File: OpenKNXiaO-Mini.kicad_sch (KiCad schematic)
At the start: 10 parts, among them J1 Conn_KNX, J5 Conn_01x05, J6 Conn_01x05, J7 Conn_01x12, SW1 Prog BTN, U1 Seeeduino XIAO

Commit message: OpenKNXiaO - Final form and dimensions are now established.
Initial housing is startet. Dimensions could be changed later
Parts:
- GN1: footprint KNeoPix:NanoBCU_PinSocket_LowProfile -> KNeoPix:OpenKNX_BCU_V2.0
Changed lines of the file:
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@@
     (pin "2")
     (instances
-      (project "KNeoPiX_v1.3"
+      (project "OpenKNXiaO-Mini"
         (path "/e63e39d7-6ac0-4ffd-8aa3-1841a4541b55"
           (reference "JP4") (unit 1)
@@
     (pin "2")
     (instances
-      (project "KNeoPiX_v1.3"
+      (project "OpenKNXiaO-Mini"
         (path "/e63e39d7-6ac0-4ffd-8aa3-1841a4541b55"
           (reference "J1") (unit 1)
@@
     (pin "2")
     (instances
-      (project "KNeoPiX_v1.3"
+      (project "OpenKNXiaO-Mini"
         (path "/e63e39d7-6ac0-4ffd-8aa3-1841a4541b55"
           (reference "SW1") (unit 1)
@@
       (effects (font (size 1.27 1.27)) (justify left))
     )
-    (property "Footprint" "KNeoPix:NanoBCU_PinSocket_LowProfile" (at 23.368 56.896 0)
+    (property "Footprint" "KNeoPix:OpenKNX_BCU_V2.0" (at 23.368 56.896 0)
       (effects (font (size 1.27 1.27)) hide)
     )
@@
     (pin "7")
     (instances
-      (project "KNeoPiX_v1.3"
+      (project "OpenKNXiaO-Mini"
         (path "/e63e39d7-6ac0-4ffd-8aa3-1841a4541b55"
           (reference "GN1") (unit 1)
@@
     (pin "9")
     (instances
-      (project "KNeoPiX_v1.3"
+      (project "OpenKNXiaO-Mini"
         (path "/e63e39d7-6ac0-4ffd-8aa3-1841a4541b55"
           (reference "U1") (unit 1)
@@
     (pin "9")
     (instances
-      (project "KNeoPiX_v1.3"
+      (project "OpenKNXiaO-Mini"
         (path "/e63e39d7-6ac0-4ffd-8aa3-1841a4541b55"
           (reference "J7") (unit 1)
@@
     (pin "C")
     (instances
-      (project "KNeoPiX_v1.3"
+      (project "OpenKNXiaO-Mini"
         (path "/e63e39d7-6ac0-4ffd-8aa3-1841a4541b55"
           (reference "D3") (unit 1)
@@
     (pin "5")
     (instances
-      (project "KNeoPiX_v1.3"
+      (project "OpenKNXiaO-Mini"
         (path "/e63e39d7-6ac0-4ffd-8aa3-1841a4541b55"
           (reference "J5") (unit 1)
@@
     (pin "5")
     (instances
-      (project "KNeoPiX_v1.3"
+      (project "OpenKNXiaO-Mini"
         (path "/e63e39d7-6ac0-4ffd-8aa3-1841a4541b55"
           (reference "J6") (unit 1)
@@
     (pin "2")
     (instances
-      (project "KNeoPiX_v1.3"
+      (project "OpenKNXiaO-Mini"
         (path "/e63e39d7-6ac0-4ffd-8aa3-1841a4541b55"
           (reference "C7") (unit 1)

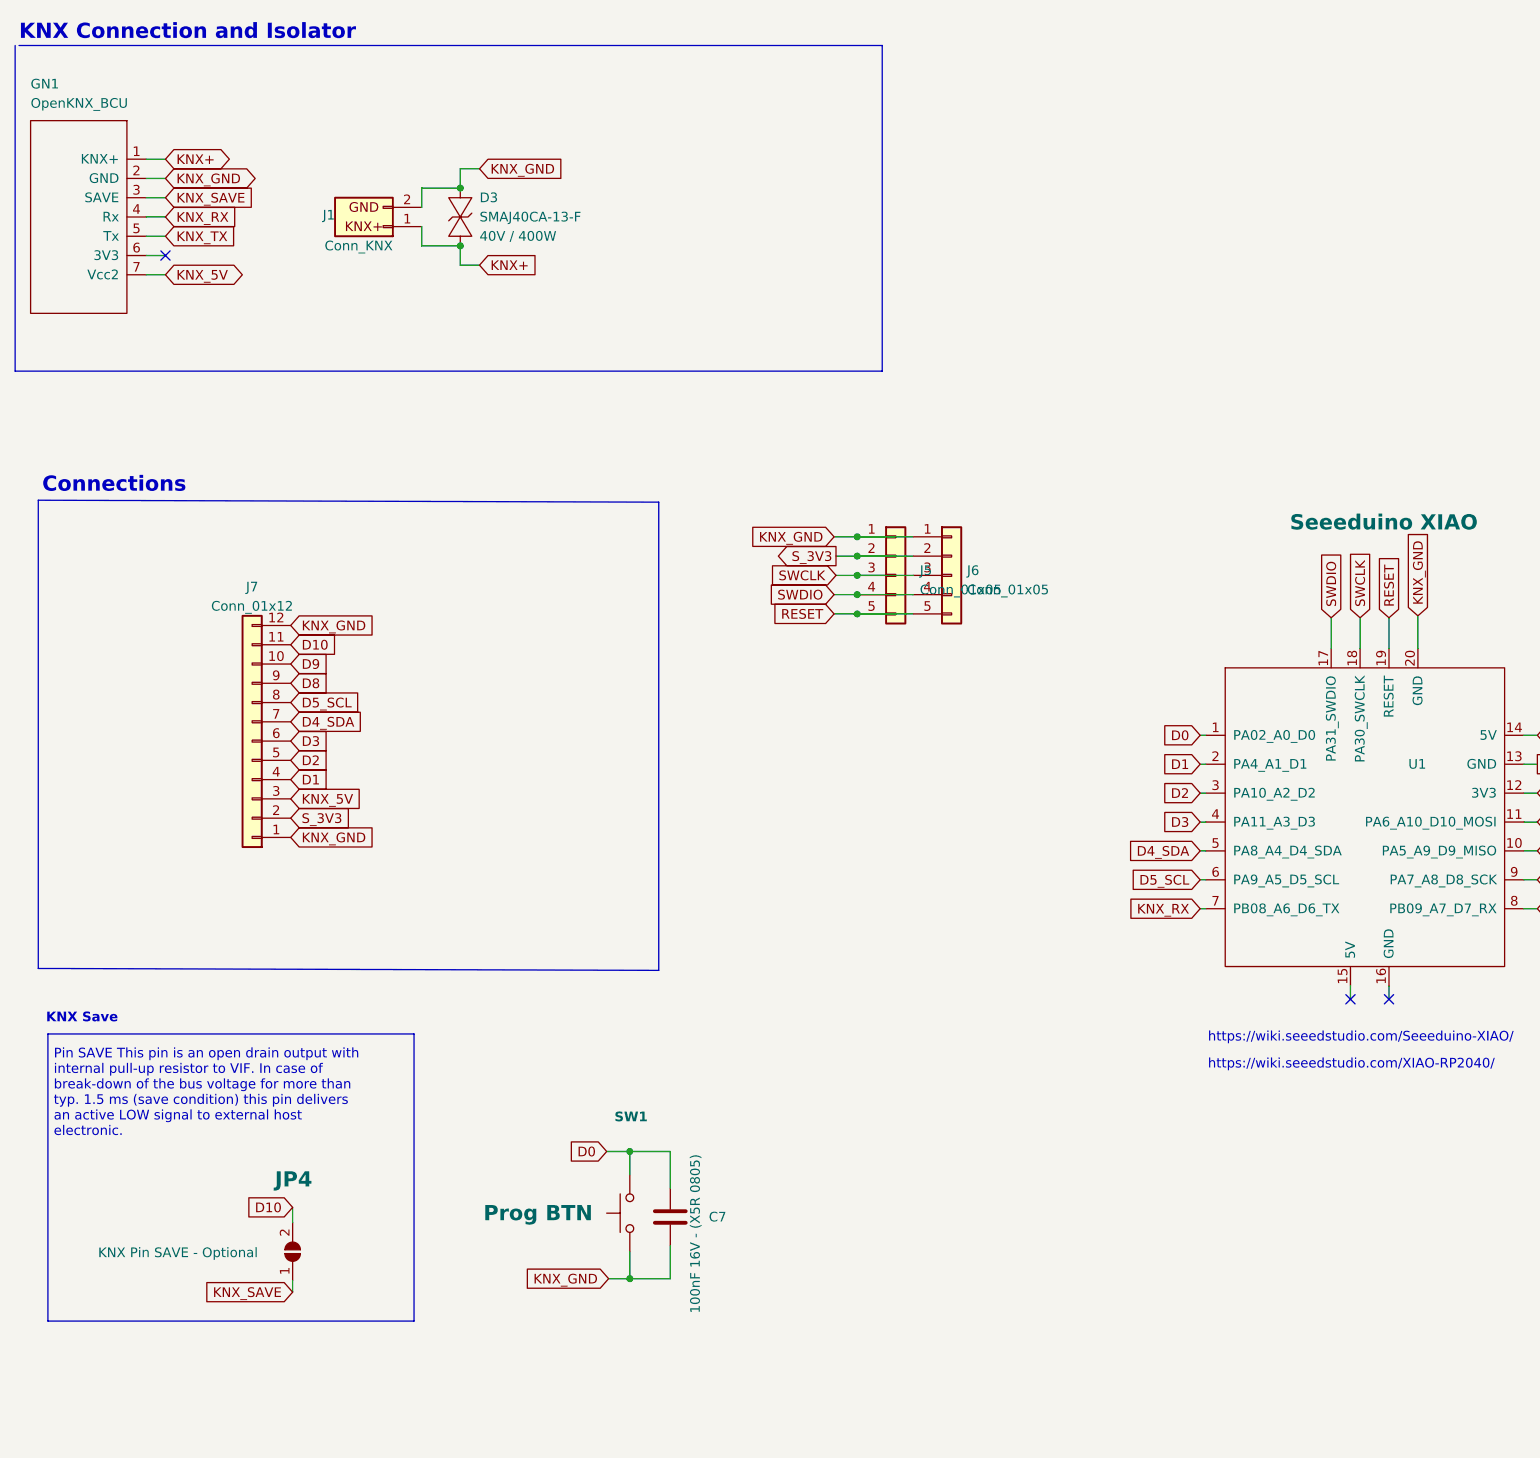
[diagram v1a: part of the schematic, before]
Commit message: Centered KNX connection and first routing
Updated low high profile (Pin-Header / Low BCU)
Removed SMA Diode. BCU has allready its own.
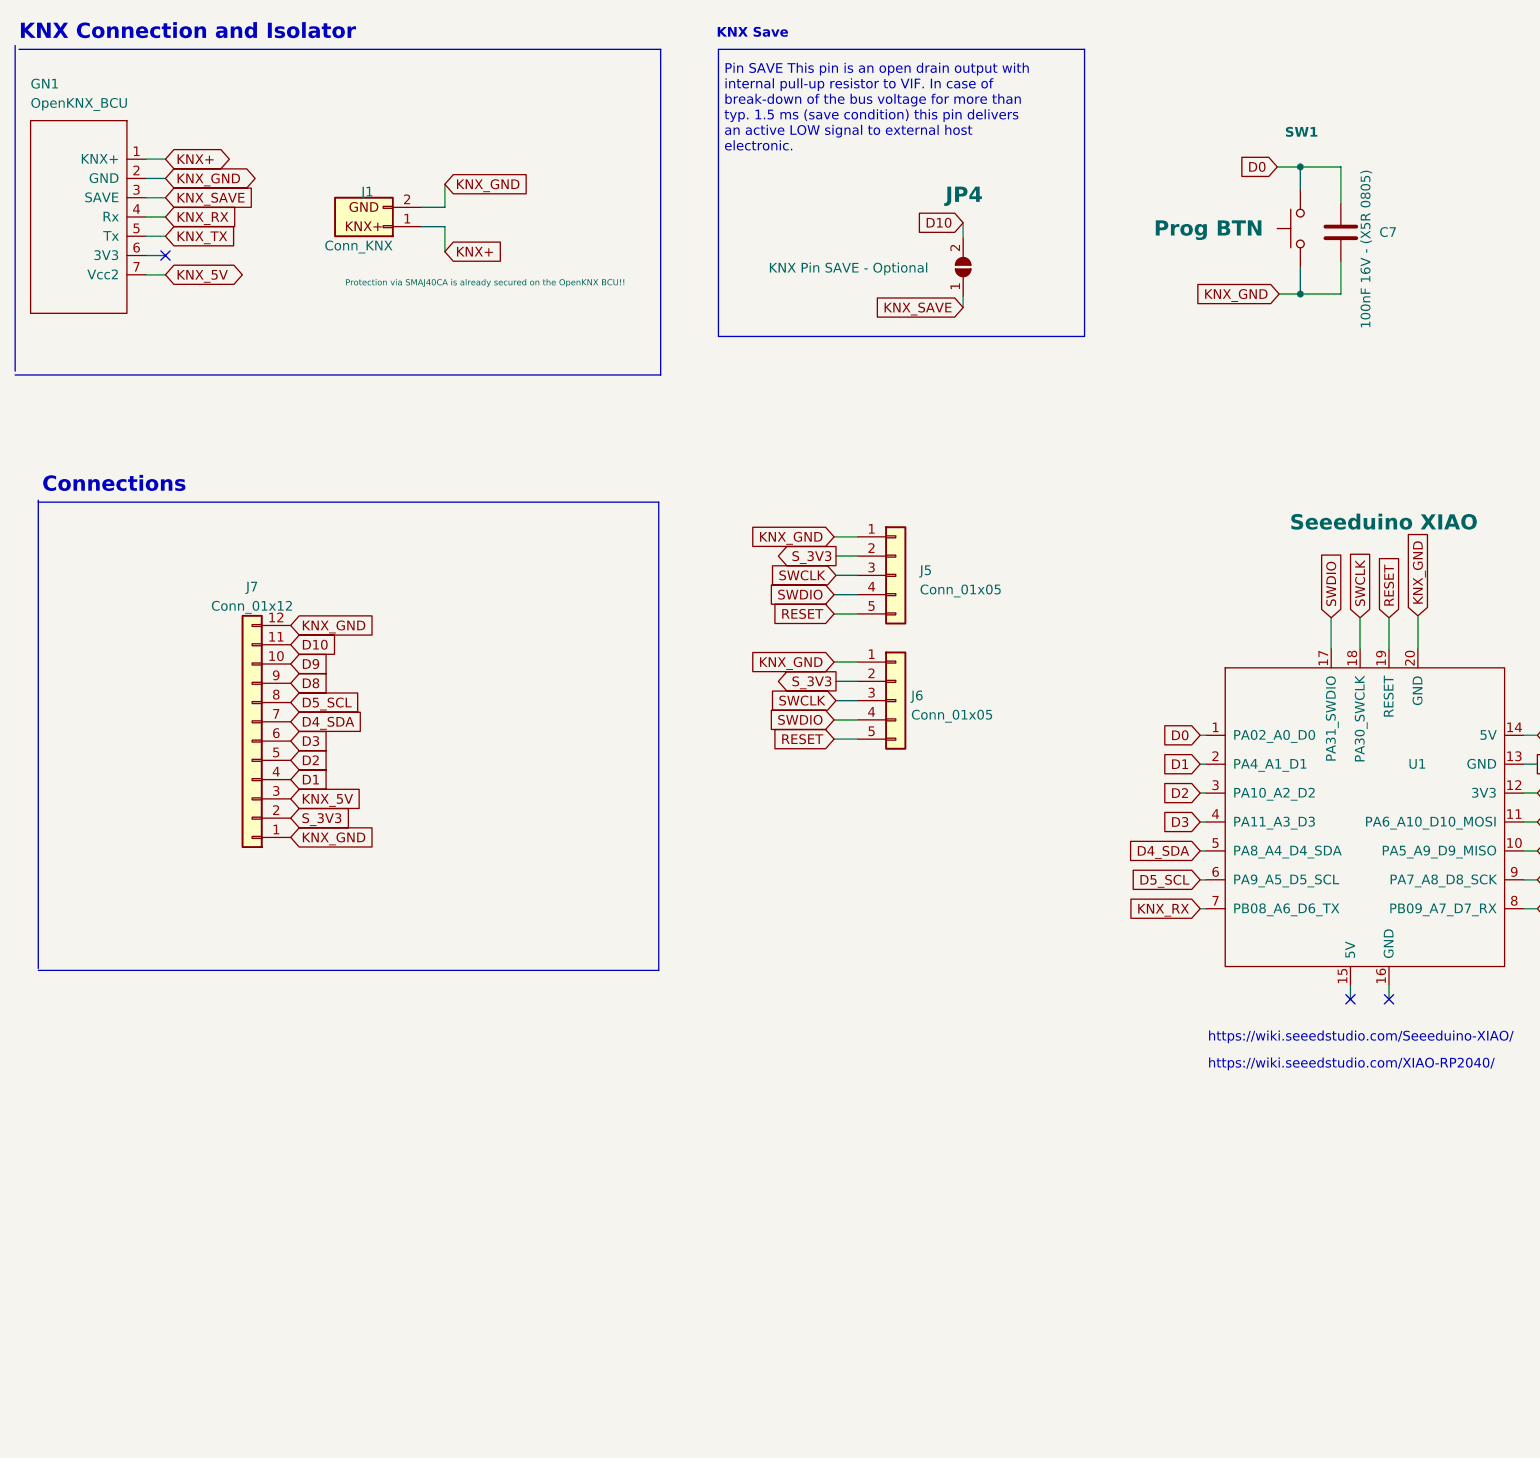
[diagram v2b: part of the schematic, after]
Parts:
- removed D3: SMAJ40CA-13-F, KNeoPix:D_SMA, symbol KNeoPix.symbols:SMAJ40CA-13-F
- J1: SMAJ40 (none) -> Protection via SMAJ40CA is already secured on the OpenKNX B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
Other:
- moved on the sheet: C7, J6, JP4, SW1

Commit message: Recheck. Add more ToDo!
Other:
- note added: "TODO for V1.4 - New Variante: - Reduce to RM1.00 CConnector JST:JST_SH_BM0 P1.00mm - Replace the 2.54 Terminal with JST! - Make is Smaler. No V-External Support! Only KNX! - Add power LED (Bus POWER) ?"
- note removed: "TODO for V1.4 - New Variante: - Reduce to RM1.00 CConnector JST:JST_SH_BM0 P1.00mm - Replace the 2.54 Terminal with JST! - Make is Smaler. No V-External Support! Only KNX!"
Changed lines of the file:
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@@
     (effects (font (size 1.27 1.27)) (justify left bottom))
   )
-  (text "TODO for V1.4 - New Variante: \n- Reduce to RM1.00 CConnector JST:JST_SH_BM0 P1.00mm\n- Replace the 2.54 Terminal with JST!\n- Make is Smaler. No V-External Support! Only KNX!\n\n"
+  (text "TODO for V1.4 - New Variante: \n- Reduce to RM1.00 CConnector JST:JST_SH_BM0 P1.00mm\n- Replace the 2.54 Terminal with JST!\n- Make is Smaler. No V-External Support! Only KNX!\n- Add power LED (Bus POWER) ?\n"
     (at 298.8056 242.2144 0)
     (effects (font (size 2 2) bold) (justify left bottom))

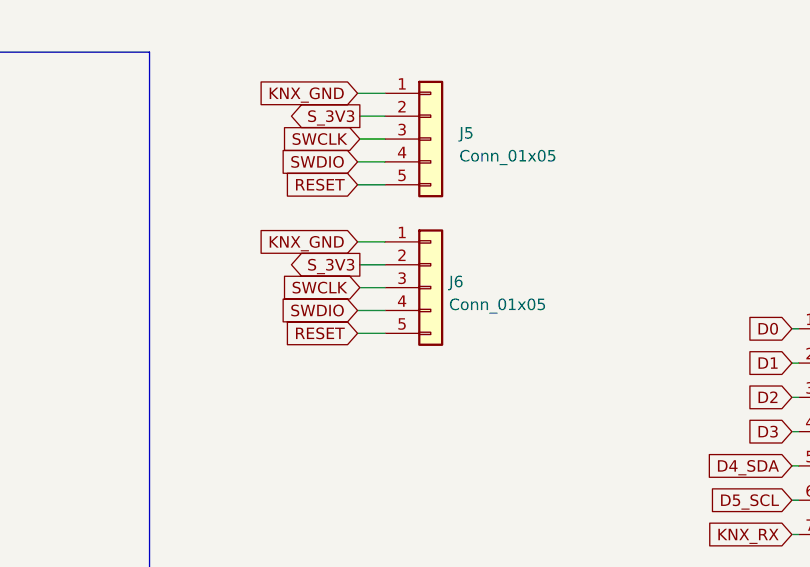
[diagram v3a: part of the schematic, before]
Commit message: rearranged Logo & Description position
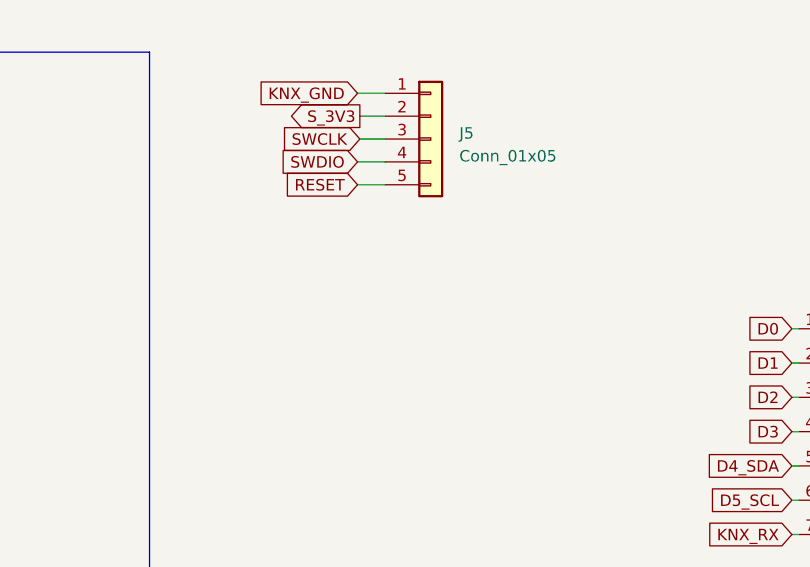
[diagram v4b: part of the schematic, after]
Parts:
- removed J6: Conn_01x05, Connector_PinHeader_1.27mm:PinHeader_1x05_P1.27mm_Vertical, symbol KNeoPix.symbols:Conn_01x05
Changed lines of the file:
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@@
-    (stroke (width 0) (type default))
-  )
-  (wire (pts (xy 125.73 106.68) (xy 128.524 106.68))
     (stroke (width 0) (type default))
   )
@@
   )
   (wire (pts (xy 202.438 98.044) (xy 202.438 102.362))
-    (stroke (width 0) (type default))
-  )
-  (wire (pts (xy 125.73 109.22) (xy 128.524 109.22))
     (stroke (width 0) (type default))
   )
@@
     (stroke (width 0) (type default))
   )
-  (wire (pts (xy 125.476 114.3) (xy 128.524 114.3))
-    (stroke (width 0) (type default))
-  )
   (wire (pts (xy 186.944 41.91) (xy 186.944 38.862))
     (stroke (width 0) (type default))
@@
   )
   (polyline (pts (xy 110.236 23.368) (xy 158.496 23.368))
-    (stroke (width 0) (type default))
-  )
-  (wire (pts (xy 125.476 104.14) (xy 128.524 104.14))
     (stroke (width 0) (type default))
   )
@@
   )
   (wire (pts (xy 193.548 148.59) (xy 193.548 146.812))
-    (stroke (width 0) (type default))
-  )
-  (wire (pts (xy 125.476 111.76) (xy 128.524 111.76))
     (stroke (width 0) (type default))
   )
@@
     )
   )
-  (global_label "SWCLK" (shape input) (at 125.73 109.22 180) (fields_autoplaced)
-    (effects (font (size 1.27 1.27)) (justify right))
-    (property "Intersheetrefs" "${INTERSHEET_REFS}" (at 116.5952 109.22 0)
-      (effects (font (size 1.27 1.27)) (justify right) hide)
-    )
-  )
   (global_label "D0" (shape input) (at 173.736 113.792 180) (fields_autoplaced)
     (effects (font (size 1.27 1.27)) (justify right))
@@
     )
   )
-  (global_label "KNX_GND" (shape input) (at 125.476 104.14 180) (fields_autoplaced)
-    (effects (font (size 1.27 1.27)) (justify right))
-    (property "Intersheetrefs" "${INTERSHEET_REFS}" (at 113.9221 104.14 0)
-      (effects (font (size 1.27 1.27)) (justify right) hide)
-    )
-  )
   (global_label "KNX+" (shape bidirectional) (at 37.338 37.846 0) (fields_autoplaced)
     (effects (font (size 1.27 1.27)) (justify left))
@@
     )
   )
-  (global_label "S_3V3" (shape output) (at 125.73 106.68 180) (fields_autoplaced)
-    (effects (font (size 1.27 1.27)) (justify right))
-    (property "Intersheetrefs" "${INTERSHEET_REFS}" (at 117.1395 106.68 0)
-      (effects (font (size 1.27 1.27)) (justify right) hide)
-    )
-  )
   (global_label "KNX_5V" (shape input) (at 218.186 113.792 0) (fields_autoplaced)
     (effects (font (size 1.27 1.27)) (justify left))
@@
     )
   )
-  (global_label "SWDIO" (shape input) (at 125.476 111.76 180) (fields_autoplaced)
-    (effects (font (size 1.27 1.27)) (justify right))
-    (property "Intersheetrefs" "${INTERSHEET_REFS}" (at 116.704 111.76 0)
-      (effects (font (size 1.27 1.27)) (justify right) hide)
-    )
-  )
   (global_label "KNX_SAVE" (shape input) (at 37.338 42.926 0) (fields_autoplaced)
     (effects (font (size 1.27 1.27)) (justify left))
@@
     (property "Intersheetrefs" "${INTERSHEET_REFS}" (at 58.7406 106.8546 0)
       (effects (font (size 1.27 1.27)) (justify left) hide)
-    )
-  )
-  (global_label "RESET" (shape input) (at 125.476 114.3 180) (fields_autoplaced)
-    (effects (font (size 1.27 1.27)) (justify right))
-    (property "Intersheetrefs" "${INTERSHEET_REFS}" (at 116.8251 114.3 0)
-      (effects (font (size 1.27 1.27)) (justify right) hide)
     )
   )
@@
         )
       )
-    )
-  )
-  (symbol (lib_id "KNeoPix.symbols:Conn_01x05") (at 133.604 109.22 0) (unit 1)
-    (in_bom yes) (on_board yes) (dnp no)
-    (property "Reference" "J6" (at 135.636 108.585 0)
-      (effects (font (size 1.27 1.27)) (justify left))
-    )
-    (property "Value" "Conn_01x05" (at 135.636 111.125 0)
-      (effects (font (size 1.27 1.27)) (justify left))
-    )
-    (property "Footprint" "Connector_PinHeader_1.27mm:PinHeader_1x05_P1.27mm_Vertical" (at 133.604 109.22 0)
-      (effects (font (size 1.27 1.27)) hide)
-    )
-    (property "Datasheet" "~" (at 133.604 109.22 0)
-      (effects (font (size 1.27 1.27)) hide)
-    )
-    (pin "1")
-    (pin "2")
-    (pin "3")
-    (pin "4")
-    (pin "5")
-    (instances
-      (project "OpenKNXiaO-Mini"
-        (path "/e63e39d7-6ac0-4ffd-8aa3-1841a4541b55"
-          (reference "J6") (unit 1)
-        )
-      )
